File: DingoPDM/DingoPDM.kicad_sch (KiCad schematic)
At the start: 6 parts

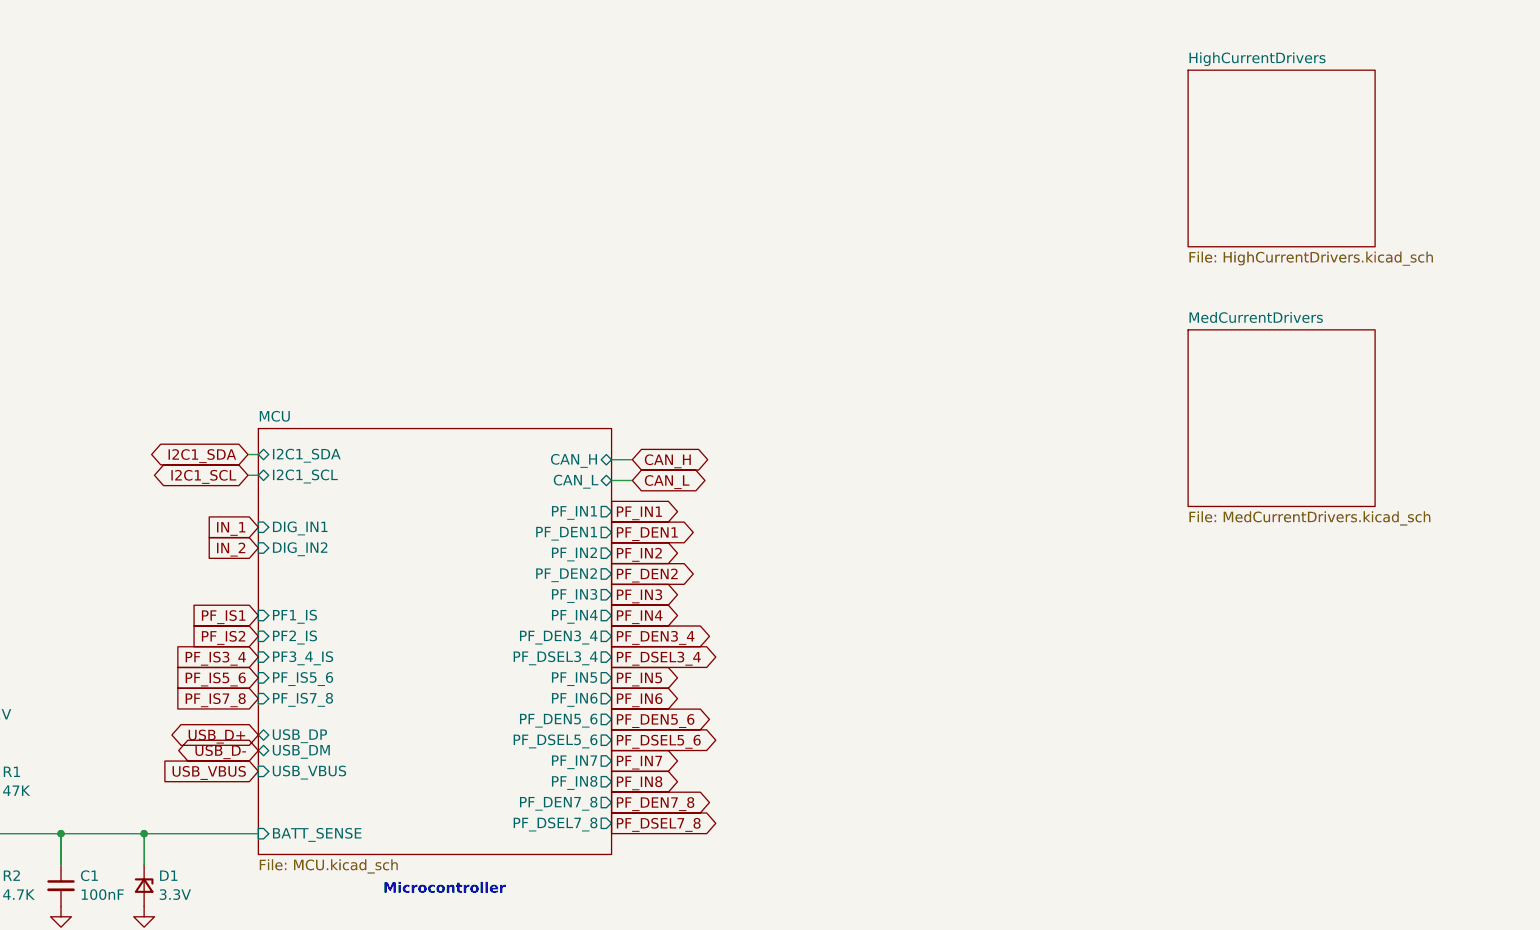
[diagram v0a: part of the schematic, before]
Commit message: Modified PCB for 10ch PDM board
I modified the original dingoPDM for 10 channels. The board has been manufactured, tested and works but after mounting I decided that it doesn't suit my needs for the current build. I may develop it further in the future, make it pretty etc but for now I am marking this project as stale.
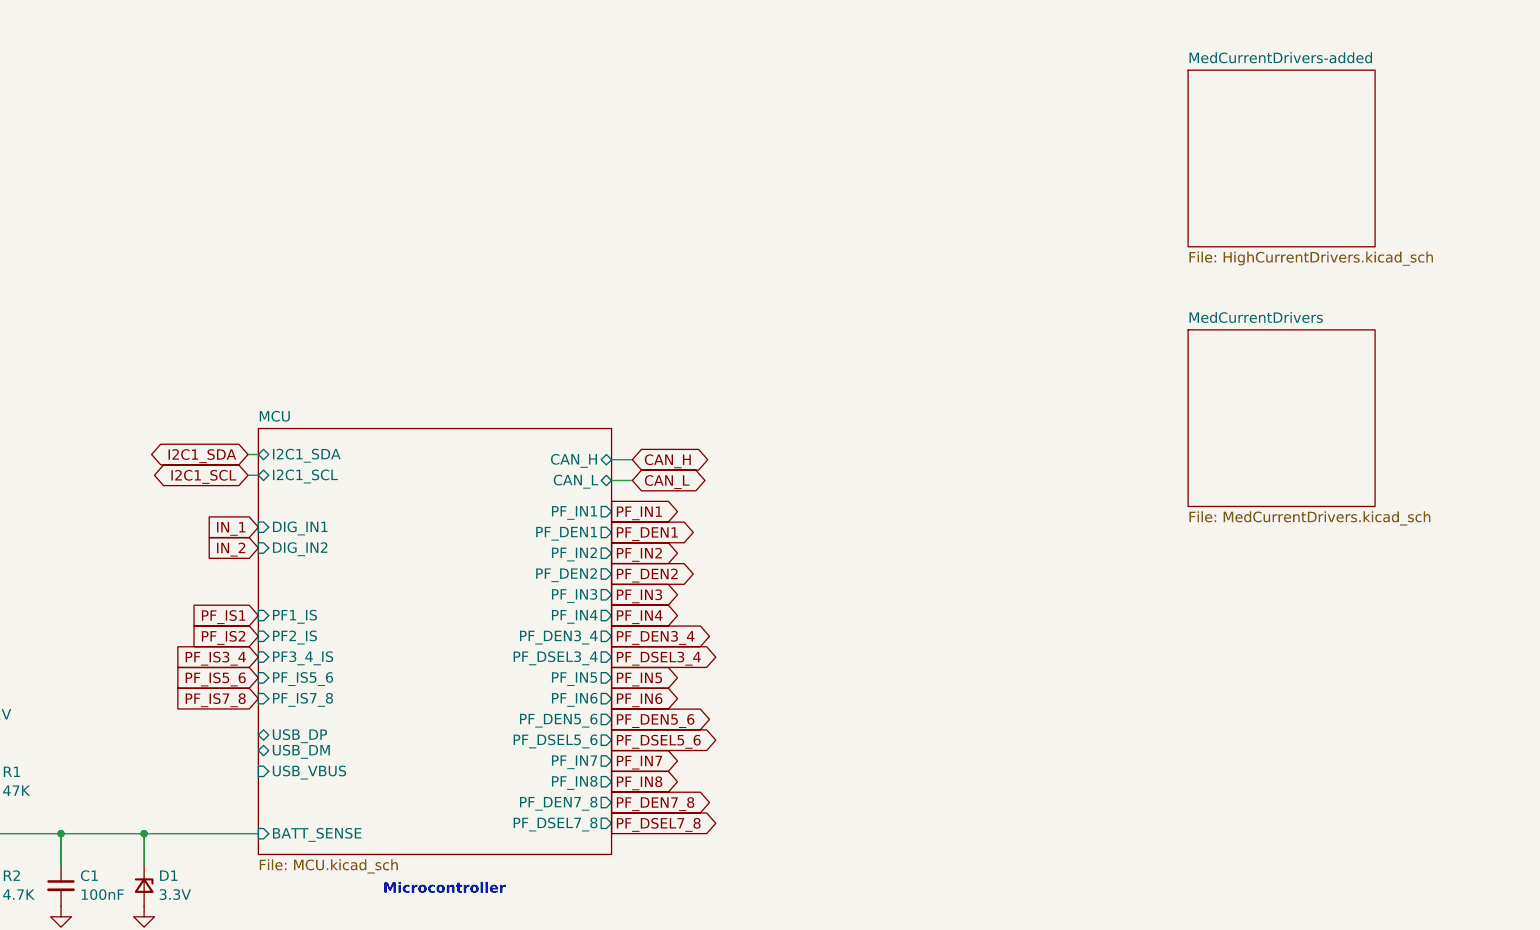
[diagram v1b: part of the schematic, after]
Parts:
- G1: footprint dingoPDM:DRTLogo -> DRTLogo:DRTLogo
- G2: footprint dingoPDM:DingoFaceNoFill -> DRTLogo:DingoFaceNoFill
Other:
- sheet HighCurrentDrivers renamed MedCurrentDrivers-added
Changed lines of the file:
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@@
-		)
-	)
-	(global_label "USB_VBUS"
-		(shape input)
-		(at 117.475 105.41 180)
-		(fields_autoplaced yes)
-		(effects
-			(font
-				(size 1.27 1.27)
-			)
-			(justify right)
-		)
-		(property "Intersheetrefs" "${INTERSHEET_REFS}"
-			(at 105.4678 105.41 0)
-			(effects
-				(font
-					(size 1.27 1.27)
-				)
-				(justify right)
-				(hide yes)
-			)
-		)
-	)
-	(global_label "USB_D-"
-		(shape bidirectional)
-		(at 117.475 102.87 180)
-		(fields_autoplaced yes)
-		(effects
-			(font
-				(size 1.27 1.27)
-			)
-			(justify right)
-		)
-		(property "Intersheetrefs" "${INTERSHEET_REFS}"
-			(at 106.5715 102.87 0)
-			(effects
-				(font
-					(size 1.27 1.27)
-				)
-				(justify right)
-				(hide yes)
-			)
 		)
 	)
@@
 		(property "Intersheetrefs" "${INTERSHEET_REFS}"
 			(at 104.2319 69.215 0)
-			(effects
-				(font
-					(size 1.27 1.27)
-				)
-				(justify right)
-				(hide yes)
-			)
-		)
-	)
-	(global_label "USB_D+"
-		(shape bidirectional)
-		(at 117.475 100.965 180)
-		(fields_autoplaced yes)
-		(effects
-			(font
-				(size 1.27 1.27)
-			)
-			(justify right)
-		)
-		(property "Intersheetrefs" "${INTERSHEET_REFS}"
-			(at 106.5715 100.965 0)
 			(effects
 				(font
@@
 			)
 		)
-		(property "Footprint" "dingoPDM:DRTLogo"
+		(property "Footprint" "DRTLogo:DRTLogo"
 			(at 252.73 157.48 0)
 			(effects
@@
 			)
 		)
-		(property "Footprint" "dingoPDM:DingoFaceNoFill"
+		(property "Footprint" "DRTLogo:DingoFaceNoFill"
 			(at 252.73 164.465 0)
 			(effects
@@
 			(color 0 0 0 0.0000)
 		)
-		(property "Sheetname" "HighCurrentDrivers"
+		(property "Sheetname" "MedCurrentDrivers-added"
 			(at 231.14 18.9734 0)
 			(effects
